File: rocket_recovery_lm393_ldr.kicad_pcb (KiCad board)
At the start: 2 copper layers, 38.2 x 57.3 mm, 19 parts, among them J1 BAT 9V, J2 TRIGGER, J3 READY, J4 ON, Q1 BC548, Q2 TIP120, U1 LM7805, U2 LM393

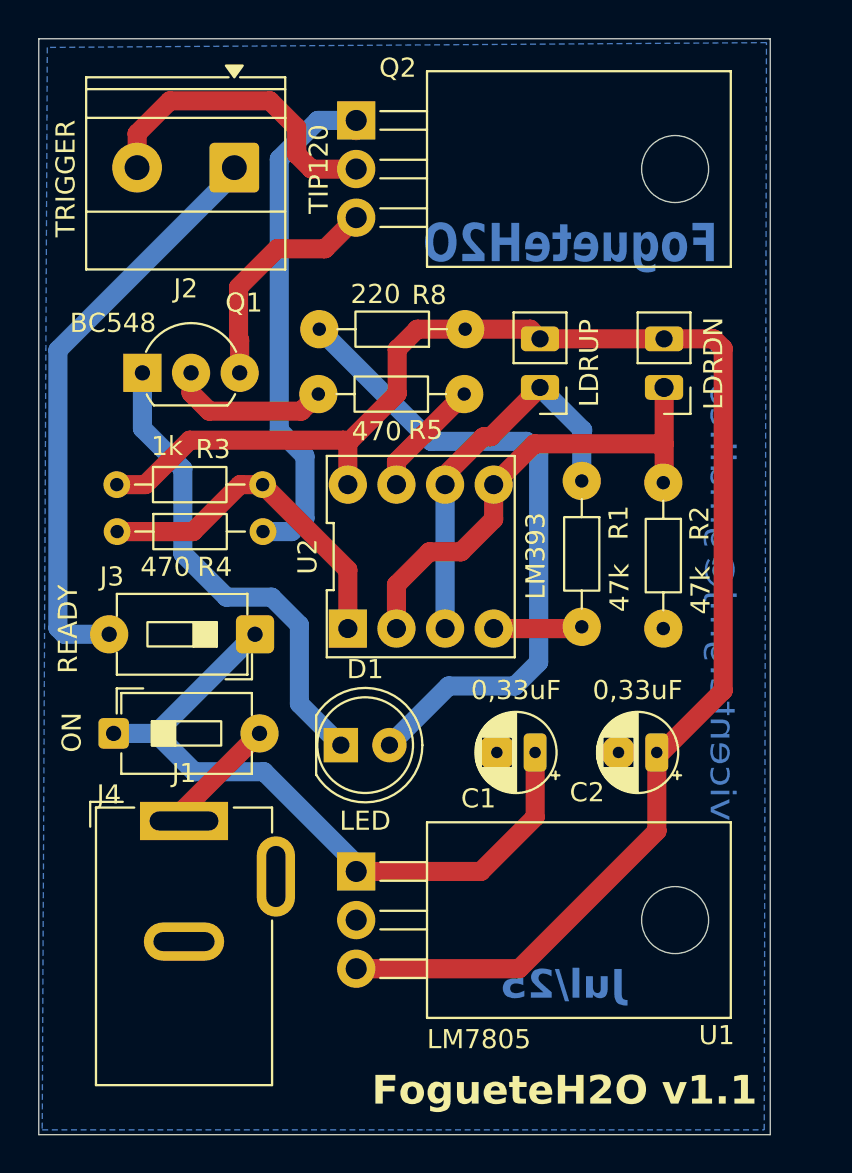
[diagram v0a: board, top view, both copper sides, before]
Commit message: Inversão sentido botão READY e ajustes de labels
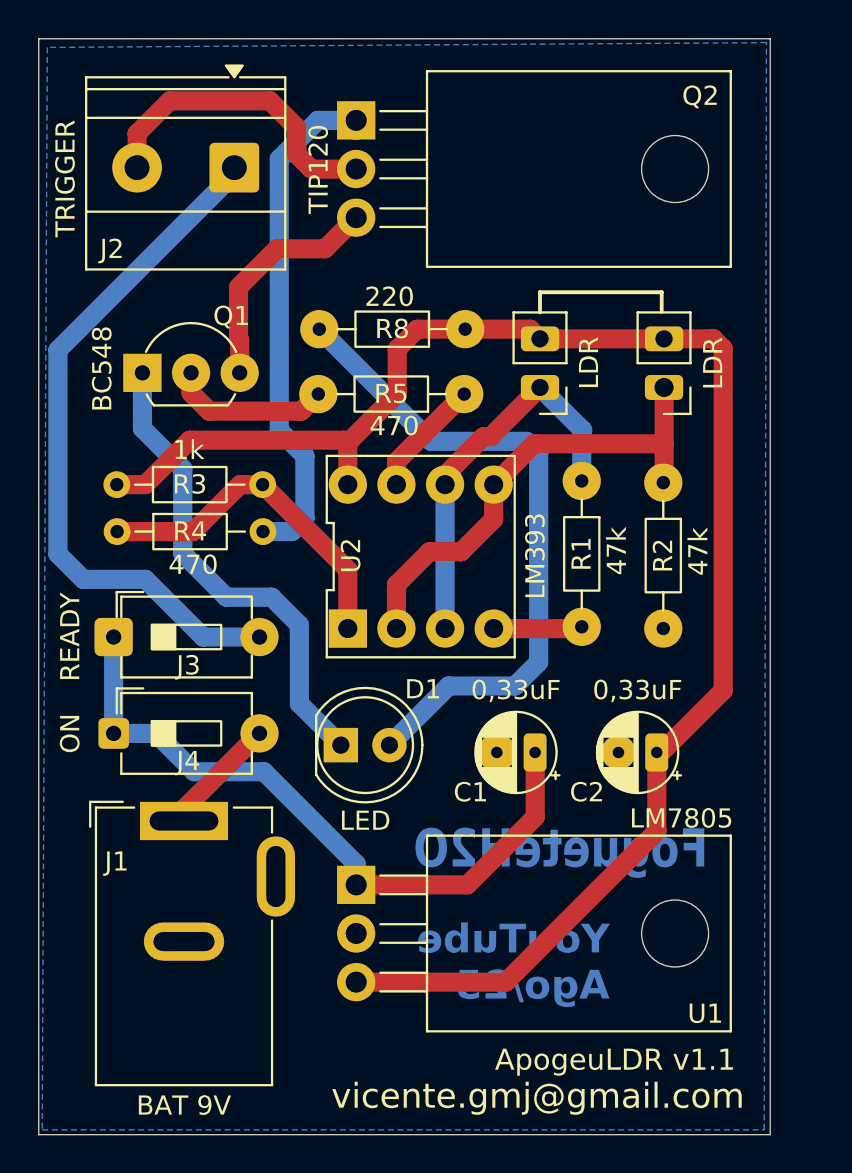
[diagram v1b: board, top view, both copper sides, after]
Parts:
- R6: value LDRUP -> LDR
- R7: value LDRDN -> LDR
- moved J3 7.39 mm to (103.3, 92.3), turned to 0 degrees
- moved U1 0.70 mm to (116.0, 105.2)
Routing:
- net Net-(J2-Pin_1): track 30.7 -> 36.3 mm
- net Net-(J3-Pin_1): track 37.1 -> 35.8 mm
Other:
- board text added: "ApogeuLDR v1.1"
- board text added: "YouTube Ago/25"
- board text removed: "FogueteH2O v1.1"
- board text removed: "Jul/25"

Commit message: Ajuste nas dimensões de furos e ilhas
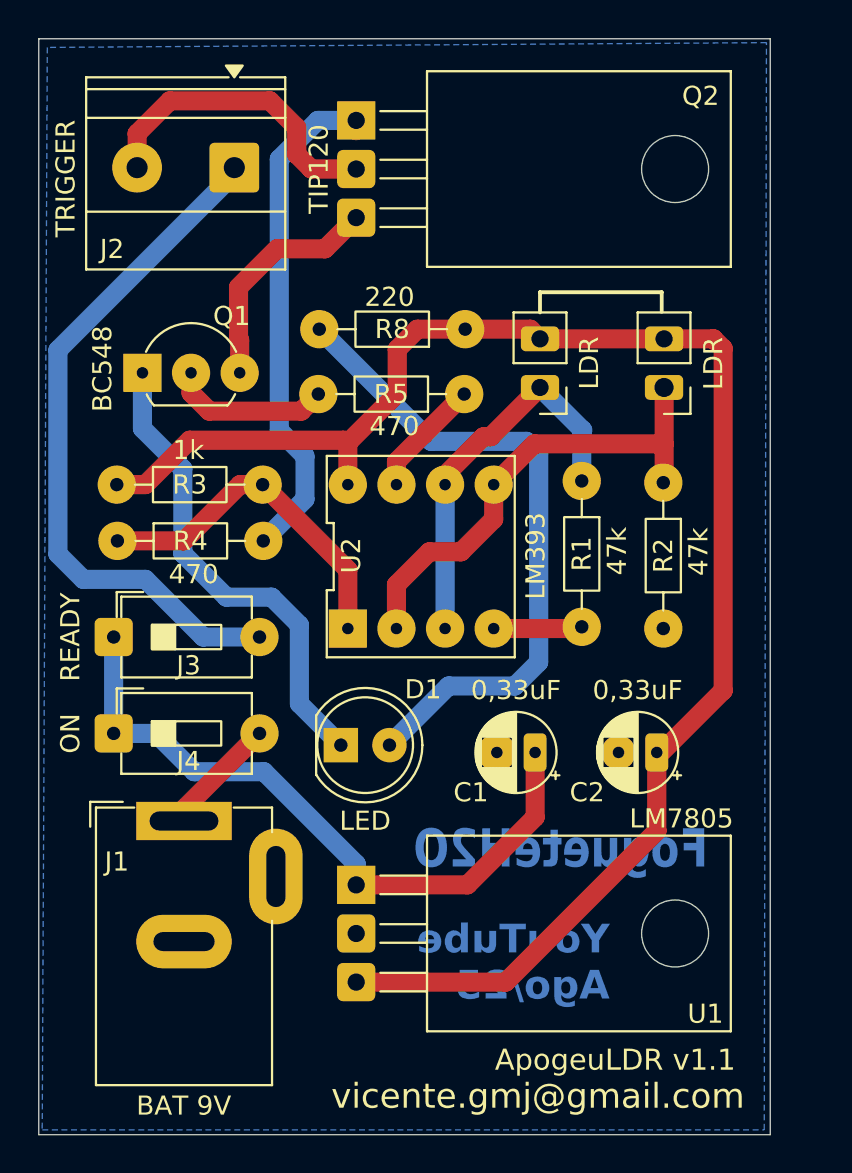
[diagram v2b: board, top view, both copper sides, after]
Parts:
- moved R4 0.49 mm to (103.5, 87.2)
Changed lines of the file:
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@@
 		(pad "1" thru_hole roundrect
 			(at 0 0)
-			(size 1.6 1.6)
-			(drill 0.8)
+			(size 2 2)
+			(drill 0.7)
 			(layers "*.Cu" "*.Mask")
 			(remove_unused_layers no)
@@
 			(at 7.62 0)
 			(size 2 2)
-			(drill 0.8)
+			(drill 0.7)
 			(layers "*.Cu" "*.Mask")
 			(remove_unused_layers no)
@@
 	(footprint "Resistor_THT:R_Axial_DIN0204_L3.6mm_D1.6mm_P7.62mm_Horizontal"
 		(layer "F.Cu")
-		(at 103.517597 86.75391)
+		(at 103.533062 87.239116)
 		(descr "Resistor, Axial_DIN0204 series, Axial, Horizontal, pin pitch=7.62mm, 0.167W, length*diameter=3.6*1.6mm^2, http://cdn-reichelt.de/documents/datenblatt/B400/1_4W%23YAG.pdf")
 		(tags "Resistor Axial_DIN0204 series Axial Horizontal pin pitch 7.62mm 0.167W length 3.6mm diameter 1.6mm")
@@
 		(pad "1" thru_hole circle
 			(at 0 0)
-			(size 1.4 1.4)
+			(size 2 2)
 			(drill 0.7)
 			(layers "*.Cu" "*.Mask")
@@
 		(pad "2" thru_hole circle
 			(at 7.62 0)
-			(size 1.4 1.4)
+			(size 2 2)
 			(drill 0.7)
 			(layers "*.Cu" "*.Mask")
@@
 			(at 0 0)
 			(size 2 2)
-			(drill 0.8)
+			(drill 0.6)
 			(layers "*.Cu" "*.Mask")
 			(remove_unused_layers no)
@@
 			(at 2.54 0)
 			(size 2 2)
-			(drill 0.8)
+			(drill 0.6)
 			(layers "*.Cu" "*.Mask")
 			(remove_unused_layers no)
@@
 			(at 5.08 0)
 			(size 2 2)
-			(drill 0.8)
+			(drill 0.6)
 			(layers "*.Cu" "*.Mask")
 			(remove_unused_layers no)
@@
 			(at 0 0 270)
 			(size 2 2)
-			(drill 1.1)
+			(drill 0.9)
 			(layers "*.Cu" "*.Mask")
 			(remove_unused_layers no)
@@
 			(pintype "input")
 		)
-		(pad "2" thru_hole oval
+		(pad "2" thru_hole roundrect
 			(at 2.54 0 270)
 			(size 2 2)
-			(drill 1.1)
+			(drill 0.9)
 			(layers "*.Cu" "*.Mask")
 			(remove_unused_layers no)
+			(roundrect_rratio 0.15625)
 			(net 8 "Net-(J2-Pin_2)")
 			(pinfunction "C")
 			(pintype "passive")
 		)
-		(pad "3" thru_hole oval
+		(pad "3" thru_hole roundrect
 			(at 5.08 0 270)
 			(size 2 2)
-			(drill 1.1)
+			(drill 0.9)
 			(layers "*.Cu" "*.Mask")
 			(remove_unused_layers no)
+			(roundrect_rratio 0.15625)
 			(net 5 "/GND")
 			(pinfunction "E")
@@
 		(pad "1" thru_hole circle
 			(at 0 0)
-			(size 1.4 1.4)
+			(size 2 2)
 			(drill 0.7)
 			(layers "*.Cu" "*.Mask")
@@
 		(pad "2" thru_hole circle
 			(at 7.62 0)
-			(size 1.4 1.4)
+			(size 2 2)
 			(drill 0.7)
 			(layers "*.Cu" "*.Mask")
@@
 			(at 0 0)
 			(size 2 2)
-			(drill 0.8)
+			(drill 0.7)
 			(layers "*.Cu" "*.Mask")
 			(remove_unused_layers no)
@@
 			(at 7.62 0)
 			(size 2 2)
-			(drill 0.8)
+			(drill 0.7)
 			(layers "*.Cu" "*.Mask")
 			(remove_unused_layers no)
@@
 			(at -3.81 3.76)
 			(size 2 2)
-			(drill 1)
+			(drill 0.6)
 			(layers "*.Cu" "*.Mask")
 			(remove_unused_layers no)
@@
 			(at -1.27 3.76)
 			(size 2 2)
-			(drill 1)
+			(drill 0.6)
 			(layers "*.Cu" "*.Mask")
 			(remove_unused_layers no)
@@
 			(at 1.27 3.76)
 			(size 2 2)
-			(drill 1)
+			(drill 0.6)
 			(layers "*.Cu" "*.Mask")
 			(remove_unused_layers no)
@@
 			(at 3.81 3.76)
 			(size 2 2)
-			(drill 1)
+			(drill 0.6)
 			(layers "*.Cu" "*.Mask")
 			(remove_unused_layers no)
@@
 			(at 3.81 -3.76)
 			(size 2 2)
-			(drill 1)
+			(drill 0.6)
 			(layers "*.Cu" "*.Mask")
 			(remove_unused_layers no)
@@
 			(at 1.27 -3.76)
 			(size 2 2)
-			(drill 1)
+			(drill 0.6)
 			(layers "*.Cu" "*.Mask")
 			(remove_unused_layers no)
@@
 			(at -1.27 -3.76)
 			(size 2 2)
-			(drill 1)
+			(drill 0.6)
 			(layers "*.Cu" "*.Mask")
 			(remove_unused_layers no)
@@
 			(at -3.81 -3.76)
 			(size 2 2)
-			(drill 1)
+			(drill 0.6)
 			(layers "*.Cu" "*.Mask")
 			(remove_unused_layers no)
@@
 		(pad "1" thru_hole rect
 			(at 0 0)
-			(size 4.6 2)
+			(size 5 2)
 			(drill oval 3.6 1)
 			(layers "*.Cu" "*.Mask")
@@
 		(pad "2" thru_hole oval
 			(at 0 6.3)
-			(size 4.2 2)
+			(size 5 2.8)
 			(drill oval 3.2 1)
 			(layers "*.Cu" "*.Mask")
@@
 		(pad "3" thru_hole oval
 			(at 4.8 2.9)
-			(size 2 4.2)
+			(size 2.8 5)
 			(drill oval 1 3.2)
 			(layers "*.Cu" "*.Mask")
@@
 			(at 0 0 180)
 			(size 2.6 2.6)
-			(drill 1.3)
+			(drill 1.1)
 			(layers "*.Cu" "*.Mask")
 			(remove_unused_layers no)
@@
 			(at 5.08 0 180)
 			(size 2.6 2.6)
-			(drill 1.3)
+			(drill 1.1)
 			(layers "*.Cu" "*.Mask")
 			(remove_unused_layers no)
@@
 			(at 0 0)
 			(size 1.8 1.8)
-			(drill 0.9)
+			(drill 0.7)
 			(layers "*.Cu" "*.Mask")
 			(remove_unused_layers no)
@@
 			(at 2.54 0)
 			(size 1.8 1.8)
-			(drill 0.9)
+			(drill 0.7)
 			(layers "*.Cu" "*.Mask")
 			(remove_unused_layers no)
@@
 			(at 0 0 270)
 			(size 2 2)
-			(drill 1.1)
+			(drill 0.9)
 			(layers "*.Cu" "*.Mask")
 			(remove_unused_layers no)
@@
 			(pintype "power_in")
 		)
-		(pad "2" thru_hole oval
+		(pad "2" thru_hole roundrect
 			(at 2.54 0 270)
 			(size 2 2)
-			(drill 1.1)
+			(drill 0.9)
 			(layers "*.Cu" "*.Mask")
 			(remove_unused_layers no)
+			(roundrect_rratio 0.15625)
 			(net 5 "/GND")
 			(pinfunction "GND")
 			(pintype "power_in")
+			(teardrops
+				(best_length_ratio 0.5)
+				(max_length 1)
+				(best_width_ratio 1)
+				(max_width 2)
+				(curved_edges no)
+				(filter_ratio 0.9)
+				(enabled yes)
+				(allow_two_segments yes)
+				(prefer_zone_connections yes)
+			)
 		)
-		(pad "3" thru_hole oval
+		(pad "3" thru_hole roundrect
 			(at 5.08 0 270)
 			(size 2 2)
-			(drill 1.1)
+			(drill 0.9)
 			(layers "*.Cu" "*.Mask")
 			(remove_unused_layers no)
+			(roundrect_rratio 0.15625)
 			(net 2 "/VCC")
 			(pinfunction "VO")
@@
 	(segment
 		(start 111.12 84.3)
-		(end 109.94 84.3)
+		(end 115.57 88.75)
 		(width 1)
 		(layer "F.Cu")
@@
 	(segment
 		(start 111.12 84.3)
-		(end 115.57 88.75)
+		(end 109.94 84.3)
 		(width 1)
 		(layer "F.Cu")
@@
 	)
 	(segment
-		(start 107.48609 86.75391)
-		(end 103.517597 86.75391)
+		(start 107.000884 87.239116)
+		(end 103.533062 87.239116)
 		(width 1)
 		(layer "F.Cu")
@@
 	(segment
 		(start 109.94 84.3)
-		(end 107.48609 86.75391)
+		(end 107.000884 87.239116)
 		(width 1)
 		(layer "F.Cu")
@@
 	)
 	(segment
-		(start 112.640771 86.75391)
-		(end 111.137597 86.75391)
+		(start 113.330054 85.062124)
+		(end 111.153062 87.239116)
 		(width 1)
 		(layer "B.Cu")
@@
 	)
 	(segment
-		(start 113.330054 86.064627)
-		(end 112.640771 86.75391)
+		(start 113.330054 82.810054)
+		(end 113.330054 85.062124)
 		(width 1)
 		(layer "B.Cu")
@@
 		(width 1)
 		(layer "B.Cu")
-		(net 7)
-	)
-	(segment
-		(start 113.330054 82.810054)
-		(end 113.330054 86.064627)
-		(width 1)
-		(layer "B.Cu")

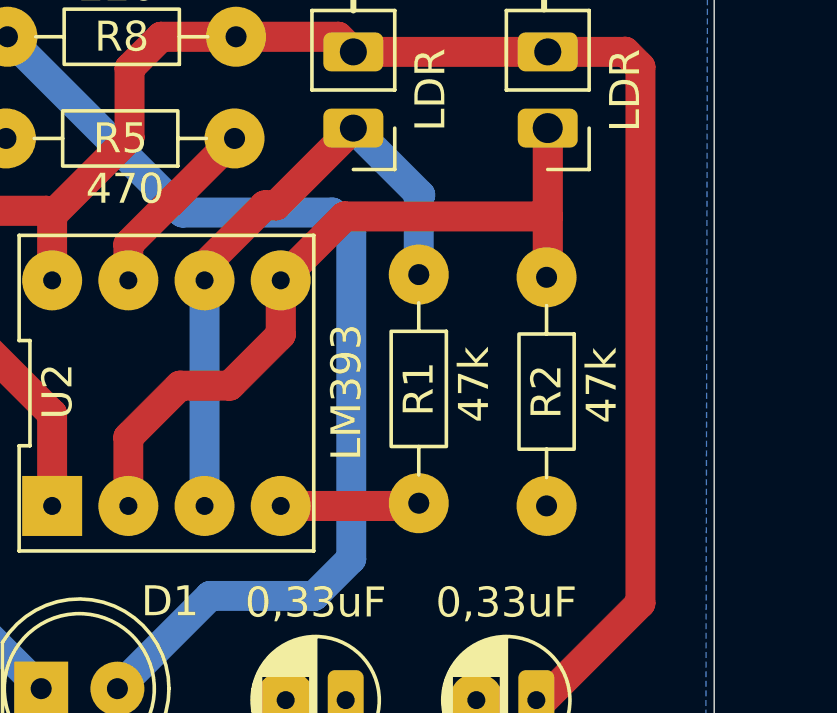
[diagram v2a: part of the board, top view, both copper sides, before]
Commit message: Excluir arquivos de backups de outra versão
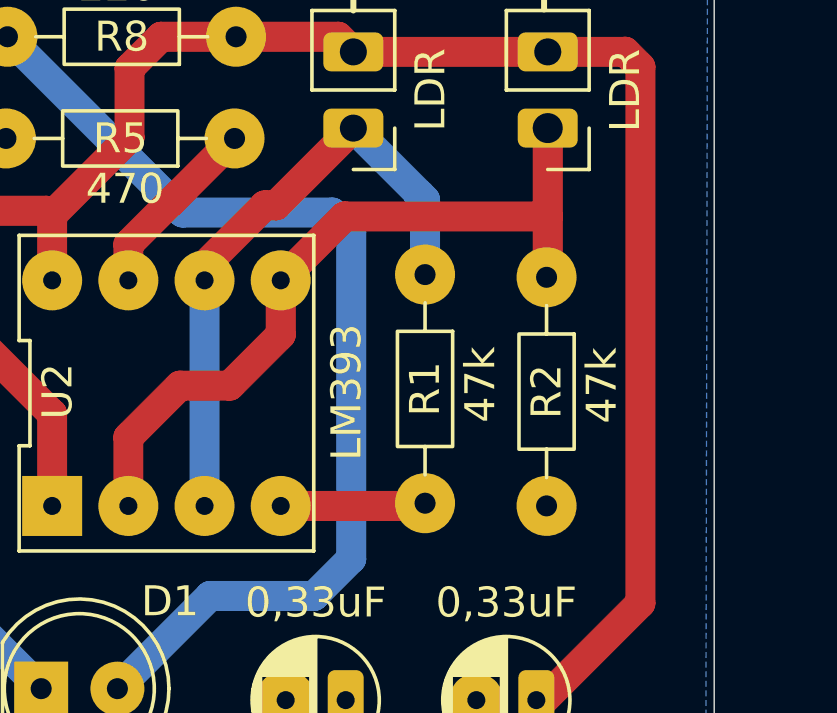
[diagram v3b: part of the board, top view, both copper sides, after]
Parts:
- moved R1 0.21 mm to (128.0, 84.1)
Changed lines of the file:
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@@
 	(footprint "Resistor_THT:R_Axial_DIN0204_L3.6mm_D1.6mm_P7.62mm_Horizontal"
 		(layer "F.Cu")
-		(at 127.790842 84.108424 -90)
+		(at 128 84.108424 -90)
 		(descr "Resistor, Axial_DIN0204 series, Axial, Horizontal, pin pitch=7.62mm, 0.167W, length*diameter=3.6*1.6mm^2, http://cdn-reichelt.de/documents/datenblatt/B400/1_4W%23YAG.pdf")
 		(tags "Resistor Axial_DIN0204 series Axial Horizontal pin pitch 7.62mm 0.167W length 3.6mm diameter 1.6mm")
 		(property "Reference" "R1"
-			(at 3.81 0 270)
+			(at 3.81 0 90)
 			(layer "F.SilkS")
 			(effects
@@
 		)
 		(property "Value" "47k"
-			(at 3.666091 -1.842716 270)
+			(at 3.666091 -1.842716 90)
 			(layer "F.SilkS")
 			(effects
@@
 		)
 		(property "Datasheet" ""
-			(at 0 0 270)
+			(at 0 0 90)
 			(layer "F.Fab")
 			(hide yes)
@@
 		)
 		(property "Description" "Resistor"
-			(at 0 0 270)
+			(at 0 0 90)
 			(layer "F.Fab")
 			(hide yes)
@@
 		)
 		(fp_text user "${REFERENCE}"
-			(at 3.81 0 270)
+			(at 3.81 0 90)
 			(layer "F.Fab")
 			(effects
@@
 	)
 	(segment
-		(start 127.790842 81.504158)
-		(end 127.790842 84.108424)
-		(width 1)
-		(layer "B.Cu")
-		(net 12)
-	)
-	(segment
 		(start 120.65 91.82)
 		(end 120.65 84.3)
 		(width 1)
 		(layer "B.Cu")
+		(net 12)
+	)
+	(segment
+		(start 128 81.615)
+		(end 128 84.108424)
+		(width 1)
+		(layer "B.Cu")
+		(net 12)
+	)
+	(segment
+		(start 127.84 81.455)
+		(end 128 81.615)
+		(width 1)
+		(layer "B.Cu")
